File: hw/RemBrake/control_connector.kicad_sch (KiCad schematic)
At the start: 8 parts, among them J4 Conn_01x08_MountingPin, J5 Conn_01x04_MountingPin, J6 Conn_01x03_MountingPin

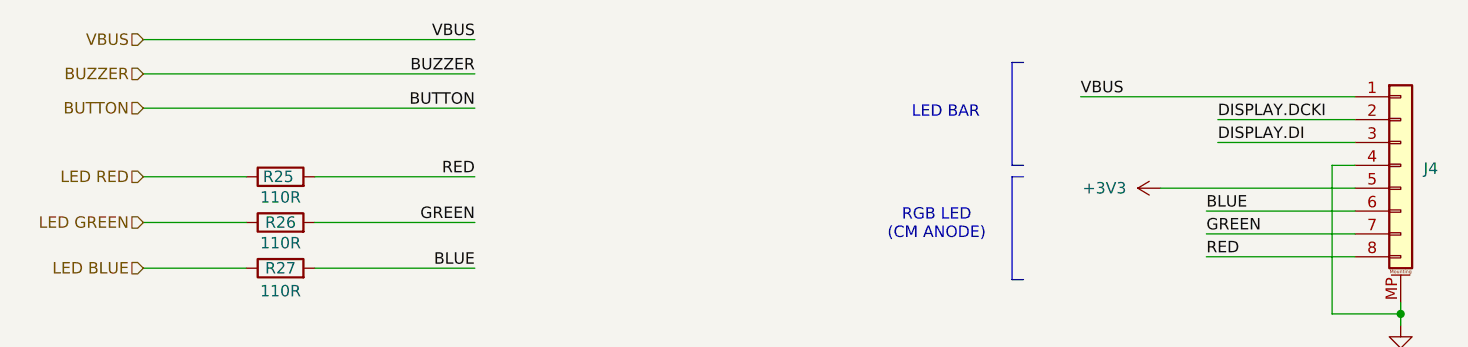
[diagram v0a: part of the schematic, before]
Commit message: added diodes to connect voltages to display and remote button even when connected to charger
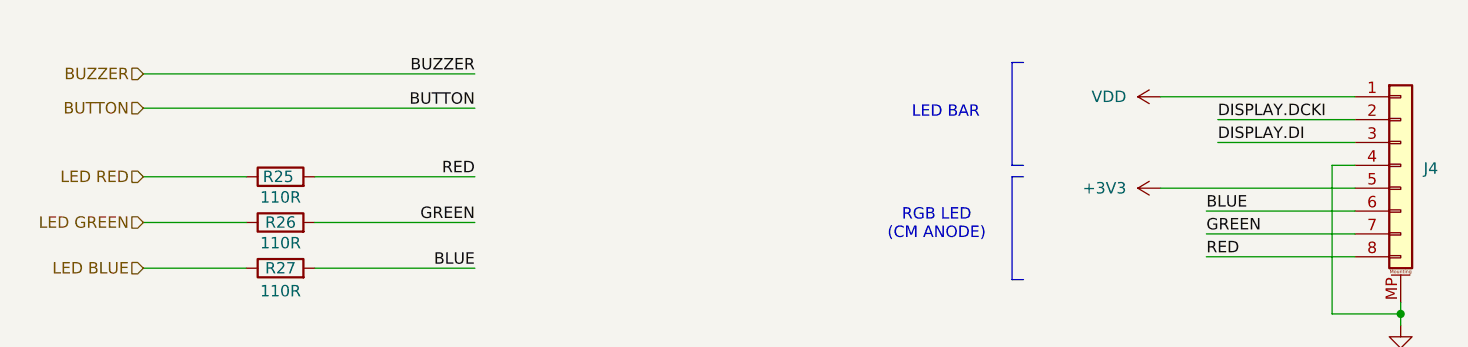
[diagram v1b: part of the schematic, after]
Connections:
- net VBUS renamed VDD
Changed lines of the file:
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@@
+	(wire
+		(pts
+			(xy 190.5 58.42) (xy 212.09 58.42)
+		)
+		(stroke
+			(width 0)
+			(type default)
+		)
+	)
 	(wire
 		(pts
@@
 		)
 	)
-	(wire
-		(pts
-			(xy 77.47 52.07) (xy 114.3 52.07)
-		)
-		(stroke
-			(width 0)
-			(type default)
-		)
-	)
-	(wire
-		(pts
-			(xy 181.61 58.42) (xy 212.09 58.42)
-		)
-		(stroke
-			(width 0)
-			(type default)
-		)
-	)
 	(polyline
 		(pts
@@
 			(width 0)
 			(type default)
-		)
-	)
-	(label "VBUS"
-		(at 114.3 52.07 180)
-		(effects
-			(font
-				(size 1.27 1.27)
-			)
-			(justify right bottom)
 		)
 	)
@@
 	(label "I2C.SCL"
 		(at 199.39 101.6 0)
-		(effects
-			(font
-				(size 1.27 1.27)
-			)
-			(justify left bottom)
-		)
-	)
-	(label "VBUS"
-		(at 181.61 58.42 0)
 		(effects
 			(font
@@
 		(shape input)
 		(at 77.47 55.88 180)
-		(effects
-			(font
-				(size 1.27 1.27)
-			)
-			(justify right)
-		)
-	)
-	(hierarchical_label "VBUS"
-		(shape input)
-		(at 77.47 52.07 180)
 		(effects
 			(font
@@
 		(dnp no)
 		(fields_autoplaced yes)
-		(property "Reference" "#PWR027"
+		(property "Reference" "#PWR028"
 			(at 96.52 146.05 0)
 			(hide yes)
@@
 			(project "RemBrake"
 				(path "/e6d4ae5b-c9d7-4cbe-b288-c929fdf55a75/c6fda42a-9645-46e5-b66a-57cf8664dccf"
-					(reference "#PWR027")
+					(reference "#PWR028")
 					(unit 1)
 				)
@@
 		(dnp no)
 		(fields_autoplaced yes)
-		(property "Reference" "#PWR029"
+		(property "Reference" "#PWR031"
 			(at 196.85 99.06 0)
 			(hide yes)
@@
 			(project "RemBrake"
 				(path "/e6d4ae5b-c9d7-4cbe-b288-c929fdf55a75/c6fda42a-9645-46e5-b66a-57cf8664dccf"
-					(reference "#PWR029")
+					(reference "#PWR031")
 					(unit 1)
 				)
@@
 		(dnp no)
 		(fields_autoplaced yes)
-		(property "Reference" "#PWR031"
+		(property "Reference" "#PWR033"
 			(at 217.17 120.65 0)
 			(hide yes)
@@
 			(project "RemBrake"
 				(path "/e6d4ae5b-c9d7-4cbe-b288-c929fdf55a75/c6fda42a-9645-46e5-b66a-57cf8664dccf"
-					(reference "#PWR031")
+					(reference "#PWR033")
 					(unit 1)
 				)
@@
 		(dnp no)
 		(fields_autoplaced yes)
-		(property "Reference" "#PWR030"
+		(property "Reference" "#PWR032"
 			(at 217.17 90.17 0)
 			(hide yes)
@@
 			(project "RemBrake"
 				(path "/e6d4ae5b-c9d7-4cbe-b288-c929fdf55a75/c6fda42a-9645-46e5-b66a-57cf8664dccf"
-					(reference "#PWR030")
+					(reference "#PWR032")
 					(unit 1)
 				)
@@
 	)
 	(symbol
+		(lib_id "power:VDD")
+		(at 190.5 58.42 90)
+		(unit 1)
+		(exclude_from_sim no)
+		(in_bom yes)
+		(on_board yes)
+		(dnp no)
+		(fields_autoplaced yes)
+		(property "Reference" "#PWR029"
+			(at 194.31 58.42 0)
+			(hide yes)
+			(effects
+				(font
+					(size 1.27 1.27)
+				)
+			)
+		)
+		(property "Value" "VDD"
+			(at 186.69 58.4199 90)
+			(effects
+				(font
+					(size 1.27 1.27)
+				)
+				(justify left)
+			)
+		)
+		(property "Footprint" ""
+			(at 190.5 58.42 0)
+			(hide yes)
+			(effects
+				(font
+					(size 1.27 1.27)
+				)
+			)
+		)
+		(property "Datasheet" ""
+			(at 190.5 58.42 0)
+			(hide yes)
+			(effects
+				(font
+					(size 1.27 1.27)
+				)
+			)
+		)
+		(property "Description" "Power symbol creates a global label with name \"VDD\""
+			(at 190.5 58.42 0)
+			(hide yes)
+			(effects
+				(font
+					(size 1.27 1.27)
+				)
+			)
+		)
+		(pin "1"
+		)
+		(instances
+			(project ""
+				(path "/e6d4ae5b-c9d7-4cbe-b288-c929fdf55a75/c6fda42a-9645-46e5-b66a-57cf8664dccf"
+					(reference "#PWR029")
+					(unit 1)
+				)
+			)
+		)
+	)
+	(symbol
 		(lib_id "power:GND")
 		(at 86.36 139.7 0)
@@
 		(dnp no)
 		(fields_autoplaced yes)
-		(property "Reference" "#PWR026"
+		(property "Reference" "#PWR027"
 			(at 86.36 146.05 0)
 			(hide yes)
@@
 			(project "RemBrake"
 				(path "/e6d4ae5b-c9d7-4cbe-b288-c929fdf55a75/c6fda42a-9645-46e5-b66a-57cf8664dccf"
-					(reference "#PWR026")
+					(reference "#PWR027")
 					(unit 1)
 				)
@@
 		(dnp no)
 		(fields_autoplaced yes)
-		(property "Reference" "#PWR032"
+		(property "Reference" "#PWR034"
 			(at 217.17 144.78 0)
 			(hide yes)
@@
 			(project "RemBrake"
 				(path "/e6d4ae5b-c9d7-4cbe-b288-c929fdf55a75/c6fda42a-9645-46e5-b66a-57cf8664dccf"
-					(reference "#PWR032")
+					(reference "#PWR034")
 					(unit 1)
 				)
@@
 		(dnp no)
 		(fields_autoplaced yes)
-		(property "Reference" "#PWR028"
+		(property "Reference" "#PWR030"
 			(at 194.31 68.58 0)
 			(hide yes)
@@
 			(project "RemBrake"
 				(path "/e6d4ae5b-c9d7-4cbe-b288-c929fdf55a75/c6fda42a-9645-46e5-b66a-57cf8664dccf"
-					(reference "#PWR028")
+					(reference "#PWR030")
 					(unit 1)
 				)

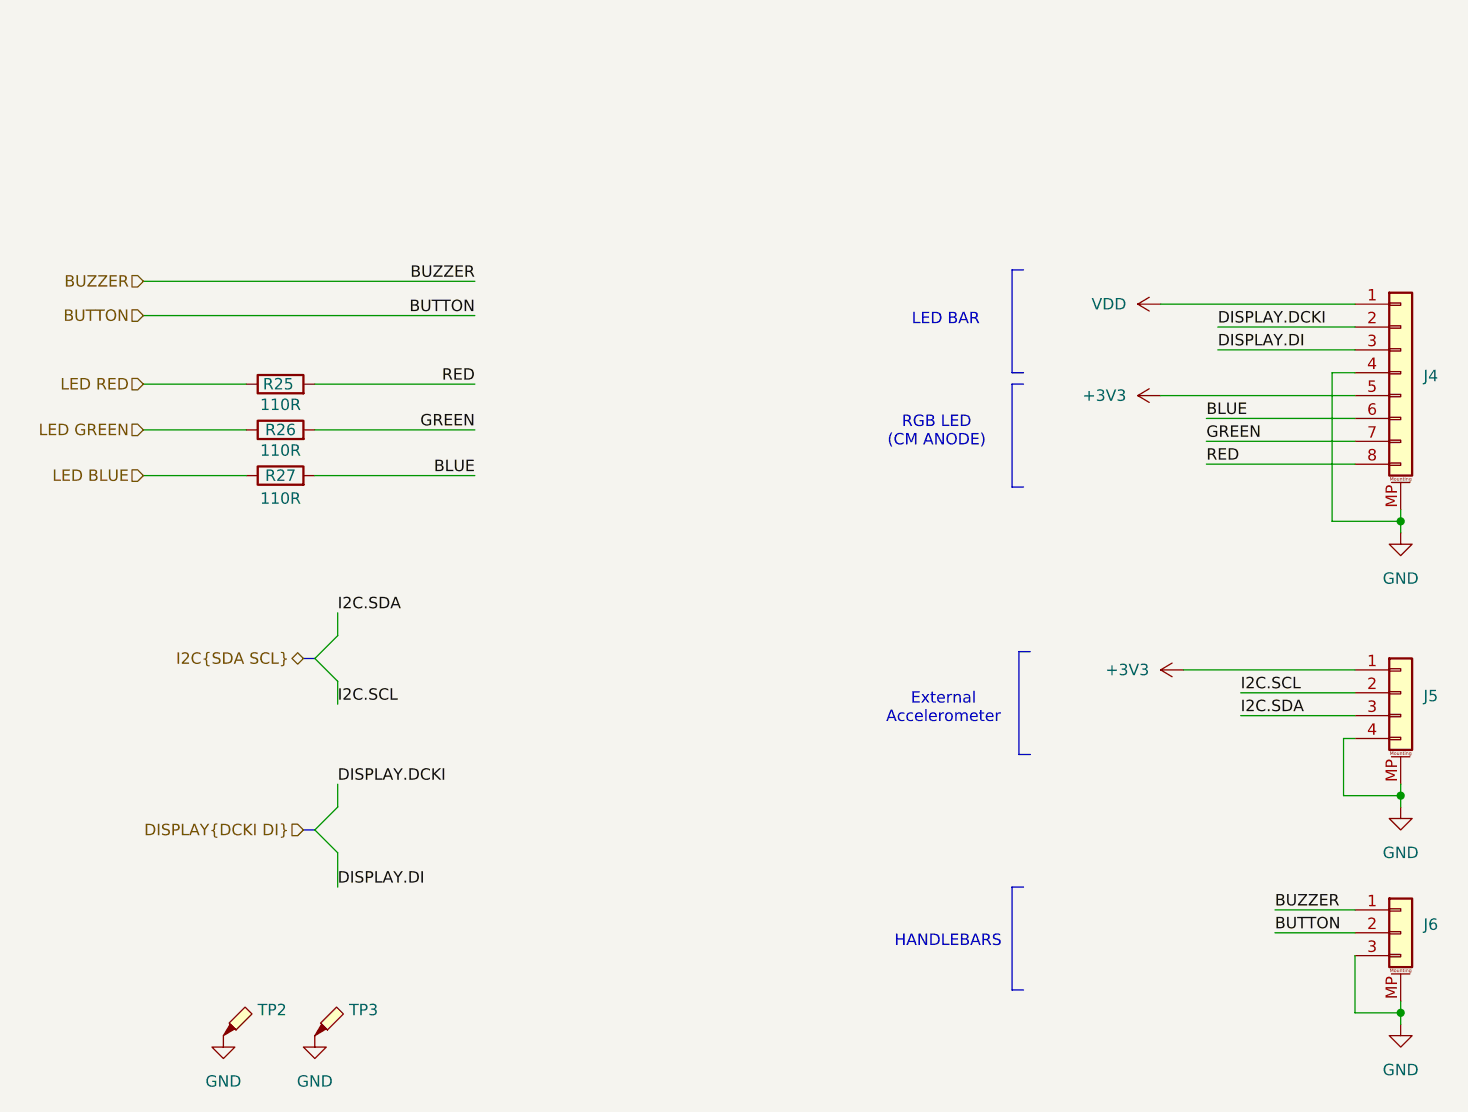
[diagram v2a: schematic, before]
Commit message: finished todos - prepared for routing
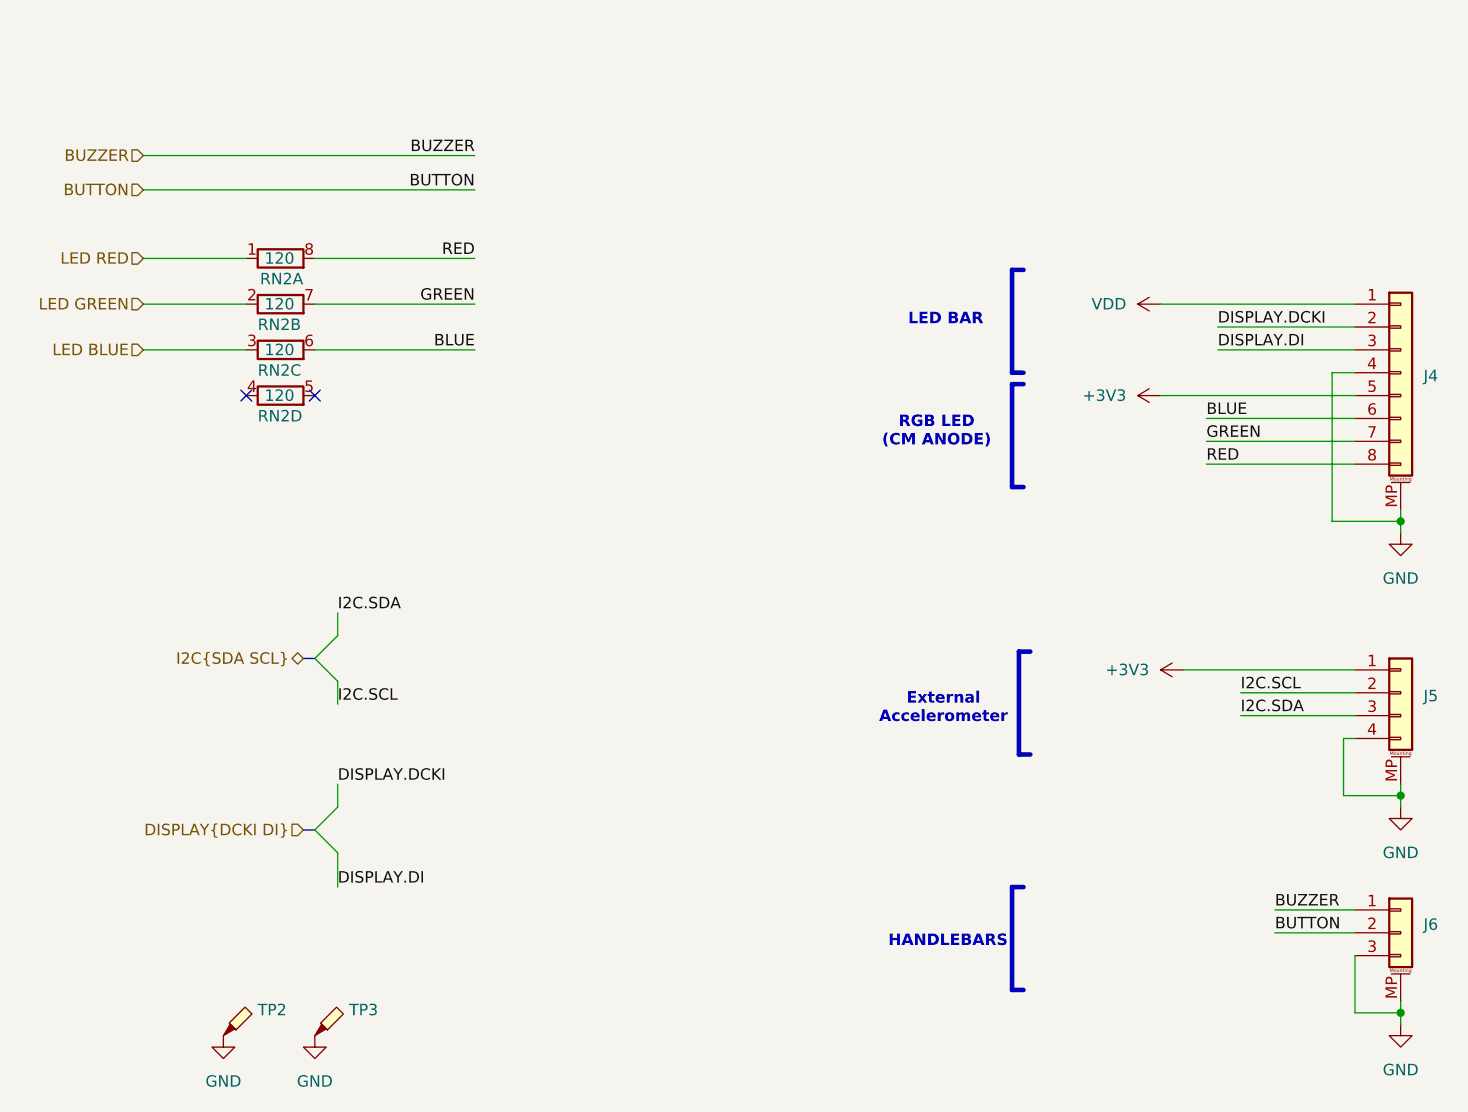
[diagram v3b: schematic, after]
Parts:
- removed R25, R26, R27: 110R, Resistor_SMD:R_0805_2012Metric_Pad1.20x1.40mm_HandSolder, symbol Device:R
- added RN2: 120, Resistor_SMD:R_Array_Concave_4x0603, symbol Device:R_Pack04_Split
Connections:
- net BLUE: now also RN2.6 (R3.2)
- net GREEN: now also RN2.7 (R2.2)
- net LED BLUE: now also RN2.3 (R3.1)
- net LED GREEN: now also RN2.2 (R2.1)
- net LED RED: now also RN2.1 (R1.1)
- net RED: now also RN2.8 (R1.2)
- no-connect marks 0 -> 2

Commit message: new routing version 3.0 with power mosfet swich for the charger and fixed problems with LED and buzzer reset delayed circuit
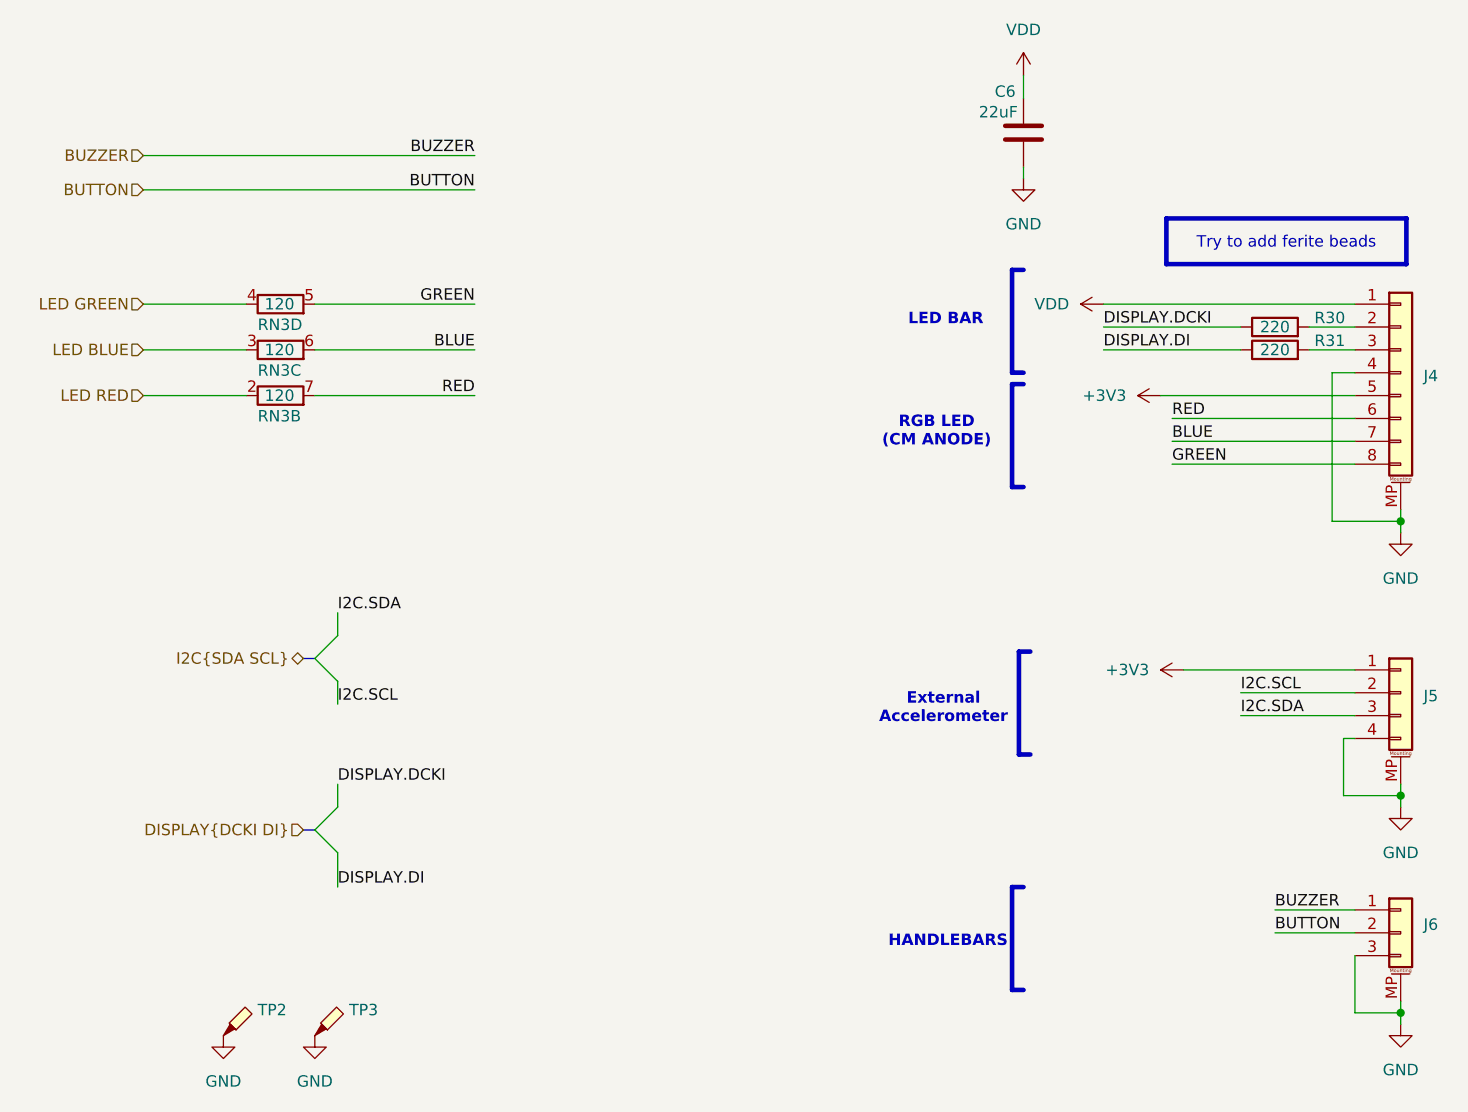
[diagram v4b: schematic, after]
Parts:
- removed unit 1 of RN2
- removed unit 3 of RN2
- removed unit 2 of RN2
- added C6: 22uF, Capacitor_SMD:C_0805_2012Metric_Pad1.18x1.45mm_HandSolder, symbol Device:C
- added R30, R31: 220, Resistor_SMD:R_0805_2012Metric_Pad1.20x1.40mm_HandSolder, symbol Device:R
- added unit 2 of RN3
- added unit 3 of RN3
- renumbered RN2 to RN3
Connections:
- net BLUE: now also J4.7 (Pin_7), RN3.6 (R3.2); no longer J4.6 (Pin_6)
- net DISPLAY.DCKI: now also R30.1; no longer J4.2 (Pin_2)
- net DISPLAY.DI: now also R31.1; no longer J4.3 (Pin_3)
- net GND: now also C6.2
- net GREEN: now also J4.8 (Pin_8), RN3.5 (R4.2); no longer J4.7 (Pin_7)
- net LED BLUE: now also RN3.3 (R3.1)
- net LED GREEN: now also RN3.4 (R4.1)
- net LED RED: now also RN3.2 (R2.1)
- net RED: now also J4.6 (Pin_6), RN3.7 (R2.2); no longer J4.8 (Pin_8)
- net VDD: now also C6.1
- new net: J4.2 (Pin_2), R30.2
- new net: J4.3 (Pin_3), R31.2
- no-connect marks 2 -> 0
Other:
- moved on the sheet: RN3D
